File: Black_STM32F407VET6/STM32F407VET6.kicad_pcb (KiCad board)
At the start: 2 copper layers, 95 parts, among them J1 T0, J10 - HotBed +, J11 Heater0, J12 X-, J13 Y-, J14 Z-, J15 Z+, J16 USB_B, J17 LeftSpi, J2 T1, J23 EXP2, J24 LCD2004, J25 Bottom, J26 Right, J28 LIGHTS, J29 Z, J3 TB, J30 Z, J38 X, J39 Y, J4 TC, J41 E0, J43 Heater1, J44 COM, J47 I2C, J48 SPI, J49 SPI, J5 + VIN -, J50 SDIO, J51 Servo, J52 Servo, J53 PowerSelect, J54 Power, J55 PD11, J56 Power, J6 Fan3, J7 Fan2, J8 Fan1, J9 Fan0, Q1 BCX70, Q10 BCX70, Q11 BCX70, Q12 IRLR8726PBF, Q13 IRLR8726PBF, Q14 IRLR8726PBF, Q2 BCX70, Q3 BCX70, Q4 IRLML0030TRPBF, Q5 BCX70, Q6 IRLML0030TRPBF, Q7 IRLML0030TRPBF, Q8 IRLML0030TRPBF, Q9 BCX70, SW1 Boot0, U1 LeftAnalog, U2 Left5V, U5 AT24CS01-SSHM

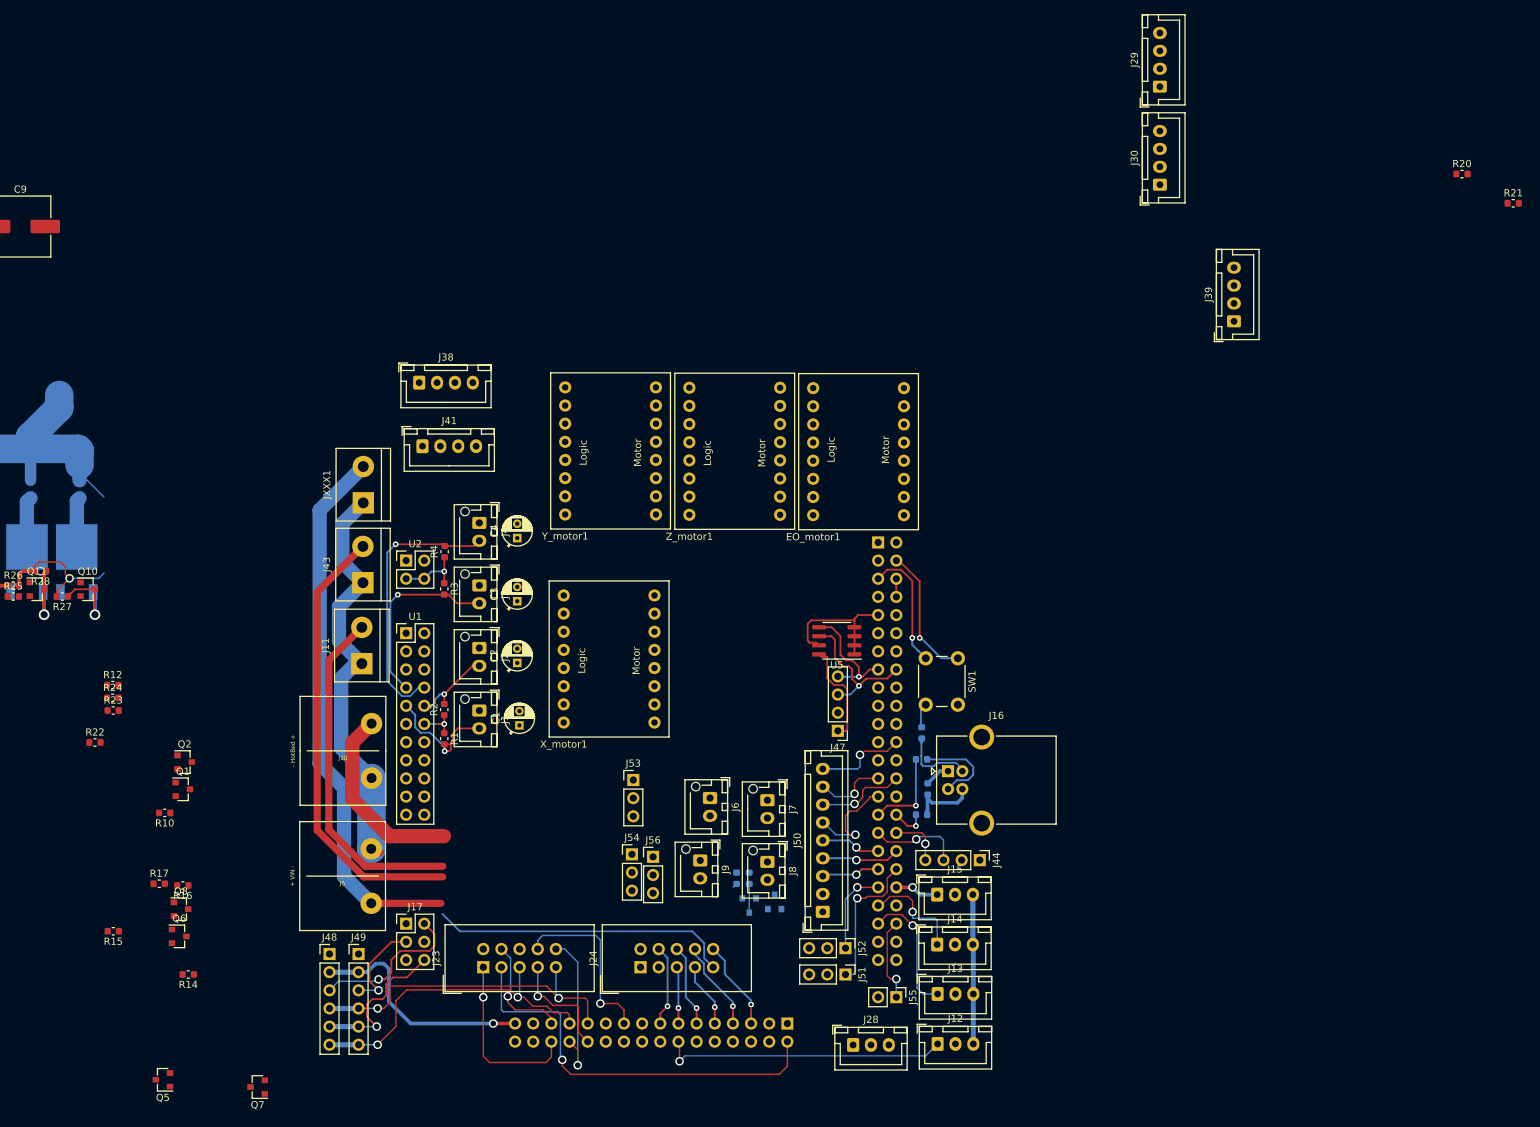
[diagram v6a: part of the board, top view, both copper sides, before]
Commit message: Layout finialized  - finished fan section  - fixed & finished temperature section  - drivers positioned roughly
Signed-off-by: Slinta <Slinta000@gmail.com>
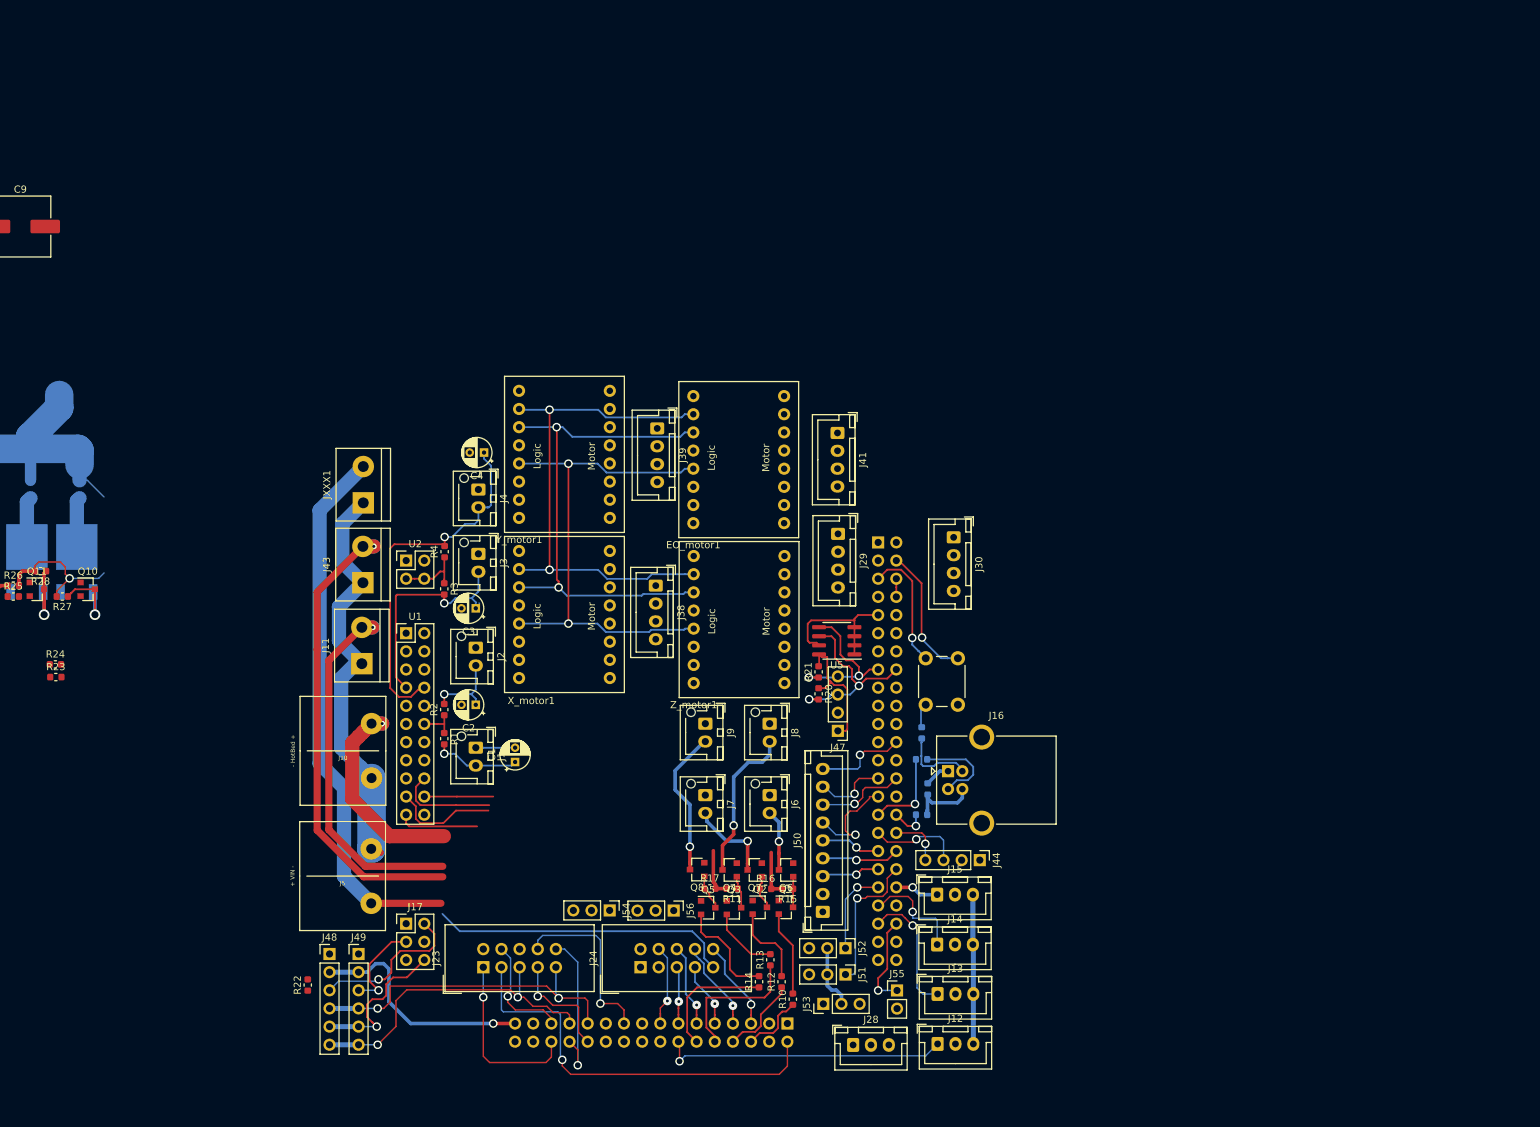
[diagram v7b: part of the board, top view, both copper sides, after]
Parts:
- Q3, Q4, R11, R13: moved to F.Cu
- moved R21 117.2 mm to (179.6, 101.9), turned to 90 degrees
- moved R20 115.7 mm to (179.6, 105.0), turned to 270 degrees
- moved R12 102.4 mm to (174.4, 145.3), turned to 90 degrees
- moved R15 94.5 mm to (175.3, 132.3)
- moved R10 91.7 mm to (176.0, 147.7), turned to 90 degrees
- moved Q1 86.0 mm to (175.1, 134.9)
- moved Q6 85.4 mm to (175.1, 129.6), turned to 180 degrees
- moved Q2 83.0 mm to (171.4, 134.9)
- moved J39 82.1 mm to (157.0, 67.9), turned to 270 degrees
- moved R16 81.5 mm to (172.2, 132.3), turned to 0 degrees
- moved Q5 80.0 mm to (164.2, 134.9), turned to 0 degrees
- moved R14 79.9 mm to (171.3, 145.3), turned to 90 degrees
- moved J29 77.1 mm to (182.3, 82.6), turned to 270 degrees
- moved R17 77.0 mm to (164.4, 132.2)
- moved Q7 75.9 mm to (170.7, 129.6)
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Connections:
- J10 pad 1: 12V -> Net-(J10-Pad1)
- Q12 pad 2: Net-(J10-Pad2) -> Net-(Q12-Pad2)
- U1 pad 13: KEYPAD_PIN -> Net-(U1-Pad13)
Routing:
- net Tmc_MISO: track 0.00 -> 87.4 mm, vias 0 -> 2
- net Tmc_SCK: track 0.00 -> 87.0 mm, vias 0 -> 2
- net Tmc_MOSI: track 0.00 -> 82.4 mm, vias 0 -> 2
- net Net-(J8-Pad2): track 0.00 -> 21.8 mm, vias 0 -> 1
- net Net-(J9-Pad2): track 0.00 -> 20.6 mm, vias 0 -> 1
- net Fan1: track 0.65 -> 19.6 mm
- net Fan0: track 0.00 -> 17.5 mm
- net Net-(Q5-Pad2): track 0.00 -> 14.8 mm
- net 12V: track 119.1 -> 132.6 mm
- net TC: track 38.3 -> 51.8 mm
- net Net-(J7-Pad2): track 0.00 -> 12.1 mm, vias 0 -> 1
- net Net-(Q1-Pad2): track 0.00 -> 11.9 mm
- net Net-(Q2-Pad2): track 0.00 -> 11.5 mm
- net Fan2: track 0.00 -> 11.4 mm
- net X_Dir: track 0.00 -> 11.3 mm
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
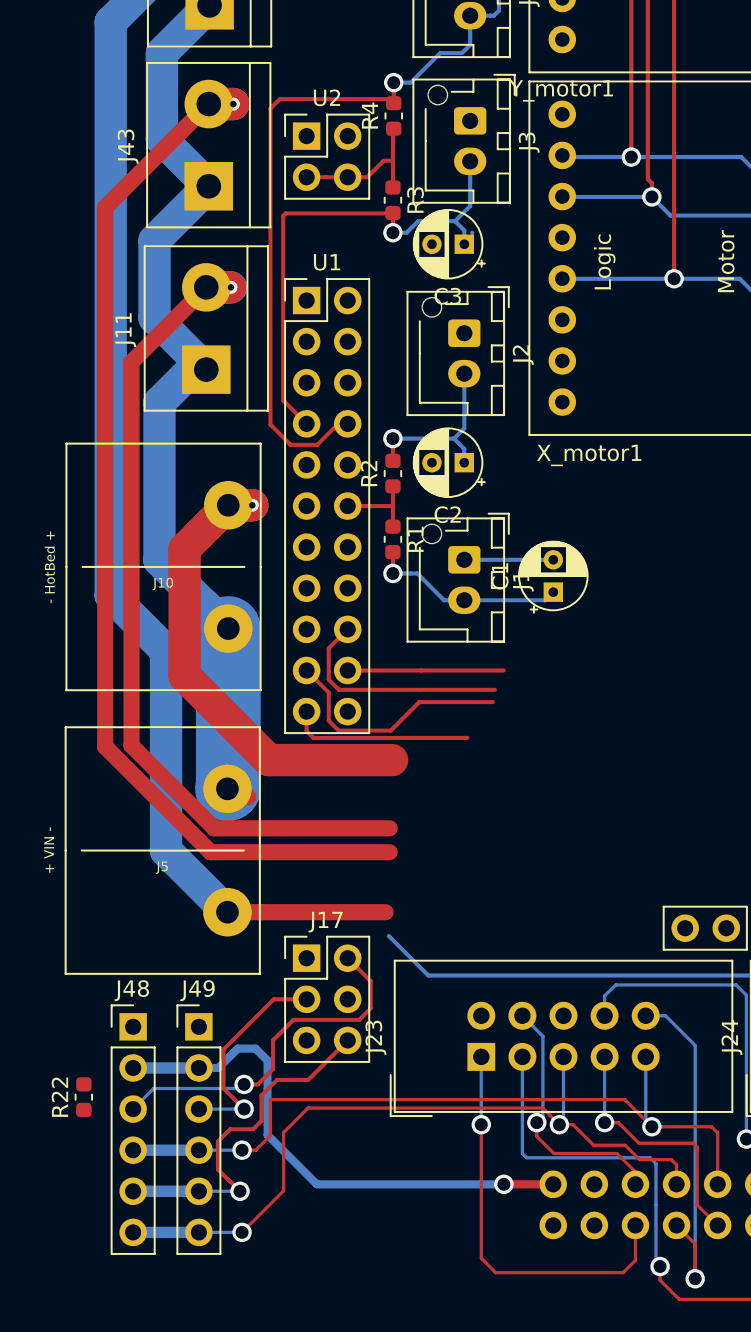
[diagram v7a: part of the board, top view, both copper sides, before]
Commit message: Changed spi channel, updated design rules TODO: change all tracks to be at least 0.25 wide and fix tracks not being in the center between headers
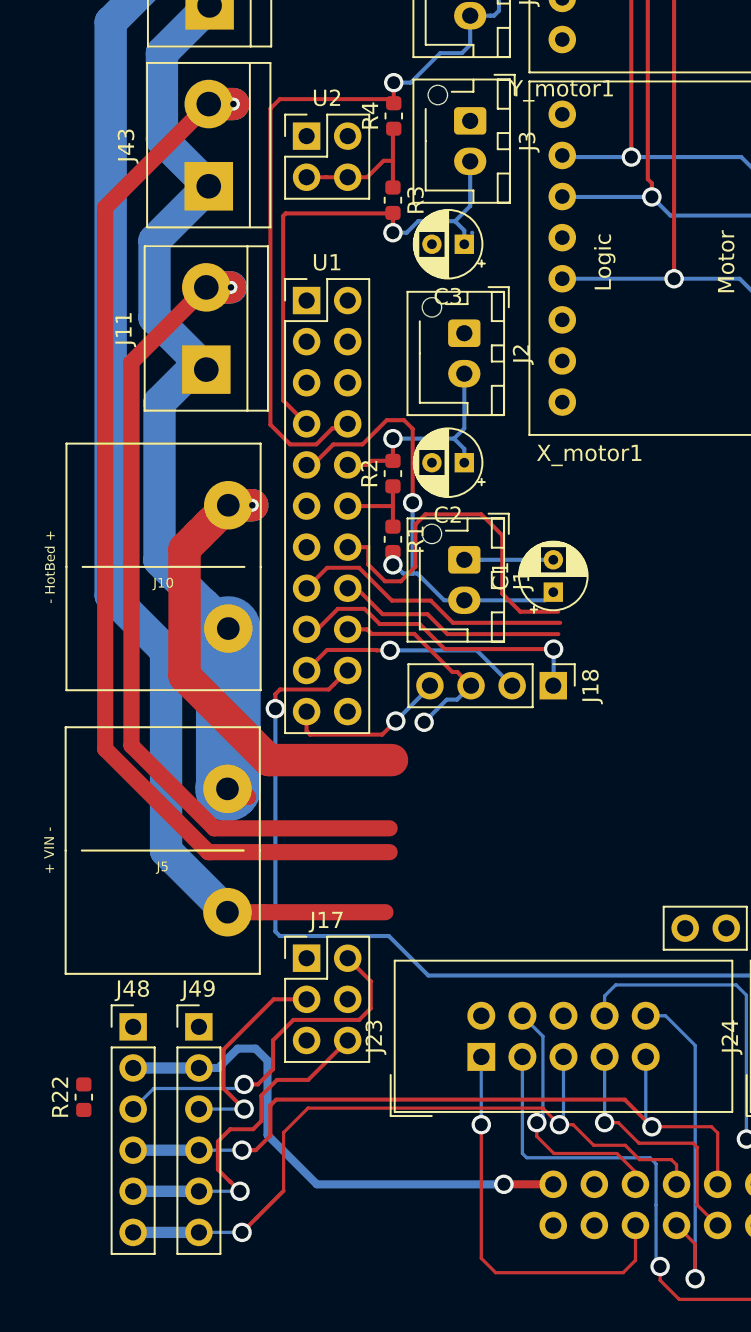
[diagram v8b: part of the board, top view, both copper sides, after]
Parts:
- added J18: EXTRAPINS, Connector_PinHeader_2.54mm:PinHeader_1x04_P2.54mm_Vertical, F.Cu at (137.2, 120.3)
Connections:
- EO_motor1 pad 2: Tmc_MOSI -> MOSI
- EO_motor1 pad 3: Tmc_SCK -> CLK
- EO_motor1 pad 5: Tmc_MISO -> MISO
- U1 pad 13: Net-(U1-Pad13) -> X_Dir
- U1 pad 17: KEYPAD_PIN -> PA4
- U1 pad 18: Tmc_SCK -> Net-(J18-Pad3)
- U1 pad 19: Tmc_MISO -> PA6
- U1 pad 20: Tmc_MOSI -> KEYPAD_PIN
- U1 pad 21: X_Dir -> PC4
- X_motor1 pad 2: Tmc_MOSI -> MOSI
- X_motor1 pad 3: Tmc_SCK -> CLK
- X_motor1 pad 5: Tmc_MISO -> MISO
- Y_motor1 pad 2: Tmc_MOSI -> MOSI
- Y_motor1 pad 3: Tmc_SCK -> CLK
- Y_motor1 pad 5: Tmc_MISO -> MISO
- Z_motor1 pad 2: Tmc_MOSI -> MOSI
- Z_motor1 pad 3: Tmc_SCK -> CLK
- Z_motor1 pad 5: Tmc_MISO -> MISO
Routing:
- net Tmc_MISO: track 87.4 -> 0.00 mm, vias 2 -> 0
- net Tmc_SCK: track 87.0 -> 0.00 mm, vias 2 -> 0
- net Tmc_MOSI: track 82.4 -> 0.00 mm, vias 2 -> 0
- net MOSI: track 45.8 -> 118.6 mm, vias 2 -> 4
- net CLK: track 47.2 -> 119.9 mm, vias 2 -> 4
- net MISO: track 43.8 -> 116.4 mm, vias 2 -> 4
- net KEYPAD_PIN: track 42.2 -> 69.1 mm, vias 0 -> 1
- net HotBed: track 0.00 -> 22.4 mm
- net PA4: track 0.00 -> 19.1 mm, vias 0 -> 1
- net Heater0: track 0.00 -> 17.6 mm
- net T0: track 12.1 -> 28.7 mm, vias 1 -> 2
- net Heater1: track 0.00 -> 14.2 mm
- net PA6: track 0.00 -> 14.1 mm, vias 0 -> 1
- net Net-(J18-Pad3): track 0.00 -> 13.7 mm, vias 0 -> 1
- net X_Dir: track 11.3 -> 0.04 mm
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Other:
- net class Default: clearance 0.2 -> 0.2925
- rule trace_clearance: 0.2 -> 0.2925
